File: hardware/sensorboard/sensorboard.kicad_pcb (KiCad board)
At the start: 2 copper layers, 48.9 x 19.3 mm, 23 parts, among them P1 PWR, P2 PROG, U1 ESP-07v2, U2 LMR16006Y, U3 BMP180_board, U4 DHT22

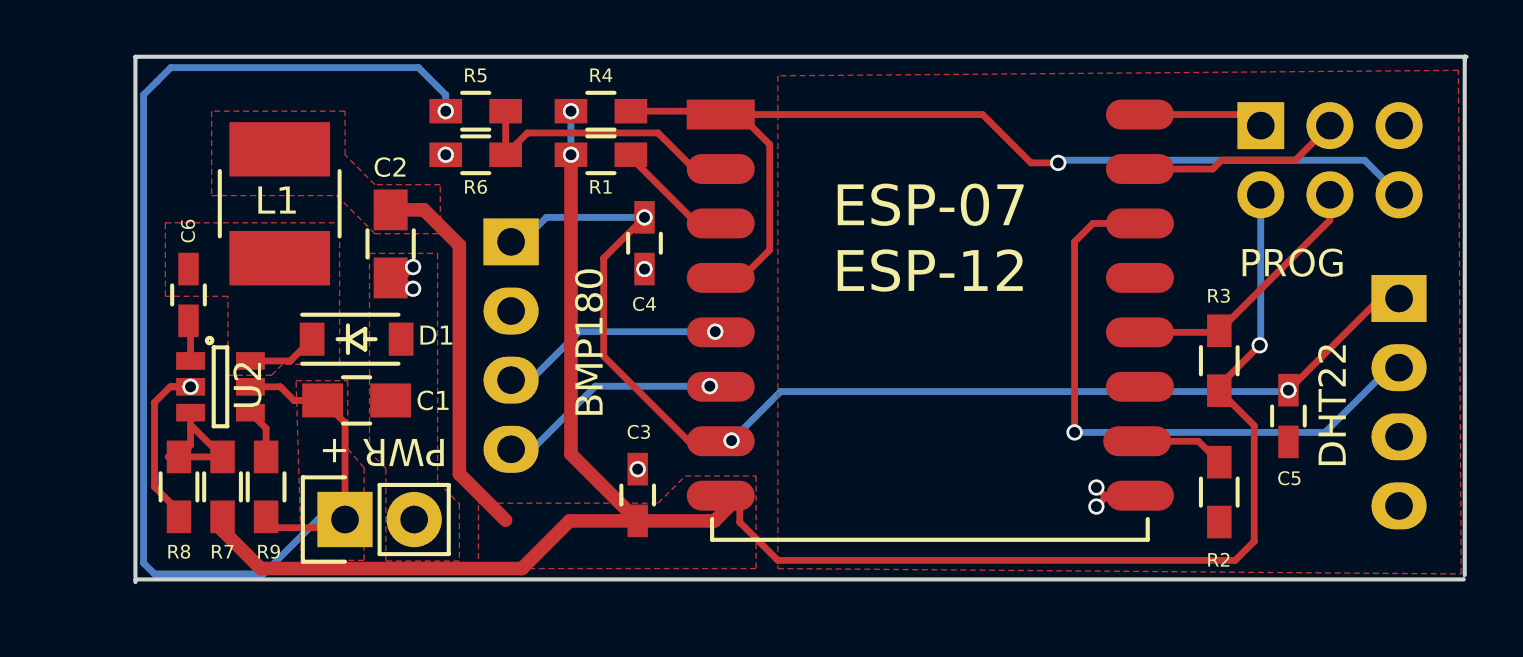
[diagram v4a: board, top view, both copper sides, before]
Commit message: Use bme280 for sensor - initial commit
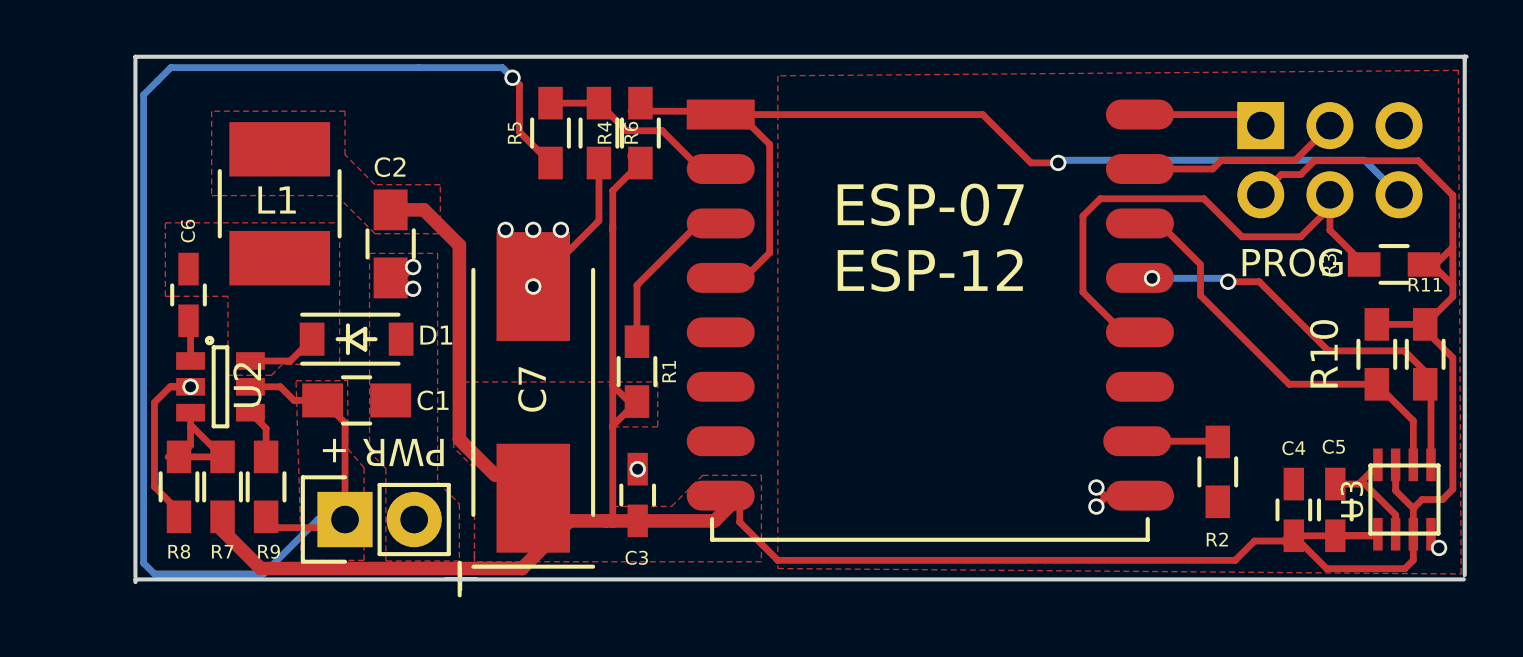
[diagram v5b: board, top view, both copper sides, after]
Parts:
- removed U4: DHT22, Pin_Headers:Pin_Header_Straight_1x04
- added C7: 100uf, Capacitors_Tantalum_SMD:TantalC_SizeD_EIA-7343_HandSoldering, F.Cu at (140.9, 84.7)
- added R10: 10k, Resistors_SMD:R_0603_HandSoldering, F.Cu at (171.9, 83.3)
- added R11: 10k, Resistors_SMD:R_0603_HandSoldering, F.Cu at (173.7, 83.3)
- U3: value BMP180_board -> BME280; footprint Pin_Headers:Pin_Header_Straight_1x04 -> TO_SOT_Packages_SMD:FGA8; moved to F.Cu
- moved U3 34.2 mm to (172.9, 88.7), turned to 0 degrees
- moved C4 25.8 mm to (168.9, 89.0), turned to 270 degrees
- moved R1 8.08 mm to (144.7, 84.0), turned to 90 degrees
- moved R3 7.33 mm to (172.5, 80.0), turned to 180 degrees
- moved R6 4.60 mm to (143.3, 75.2), turned to 270 degrees
- moved C5 3.85 mm to (170.4, 89.0), turned to 270 degrees
- moved R5 2.86 mm to (141.5, 75.2), turned to 90 degrees
- moved R4 1.66 mm to (144.9, 75.2), turned to 90 degrees
- moved R2 0.74 mm to (166.1, 87.6)
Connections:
- C4 pad 2: +3.3VP -> +3V3
- C5 pad 2: +3.3VP -> +3V3
- U1 pad 13: Net-(U1-Pad13) -> SDL
- U1 pad 14: GPIO4 -> SDA
- U1 pad 5: GPIO14 -> Net-(U1-Pad5)
- U1 pad 6: GPIO12 -> Net-(U1-Pad6)
- U1 pad 7: +3.3VP -> Net-(U1-Pad7)
- U3 pad 1: +3.3VP -> GND
- U3 pad 2: GND -> +3V3
- U3 pad 3: GPIO14 -> SDA
- U3 pad 4: GPIO12 -> SDL
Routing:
- net +3.3VP: track 44.3 -> 0.00 mm, vias 3 -> 0
- net +3V3: track 85.8 -> 111.5 mm, vias 3 -> 0
- net GPIO4: track 21.9 -> 0.00 mm, vias 1 -> 0
- net SDL: track 0.00 -> 16.5 mm, vias 0 -> 2
- net GND: track 11.4 -> 27.8 mm, vias 8 -> 11
- net SDA: track 0.00 -> 16.0 mm
- net GPIO12: track 9.36 -> 0.00 mm, vias 1 -> 0
- net GPIO14: track 9.14 -> 0.00 mm, vias 1 -> 0
- net GPIO0: track 10.3 -> 18.8 mm
- net +6V: track 48.8 -> 54.1 mm
- net CH_PD: track 5.10 -> 8.27 mm
- net ADC_IN: track 11.1 -> 9.63 mm
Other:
- board text removed: "BMP180"
- board text removed: "DATA"
- board text removed: "DHT22"
- board text removed: "SCL"
- board text removed: "SDA"
- board text removed: "VIN"

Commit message: Fix sensor placement and improve silkscreens
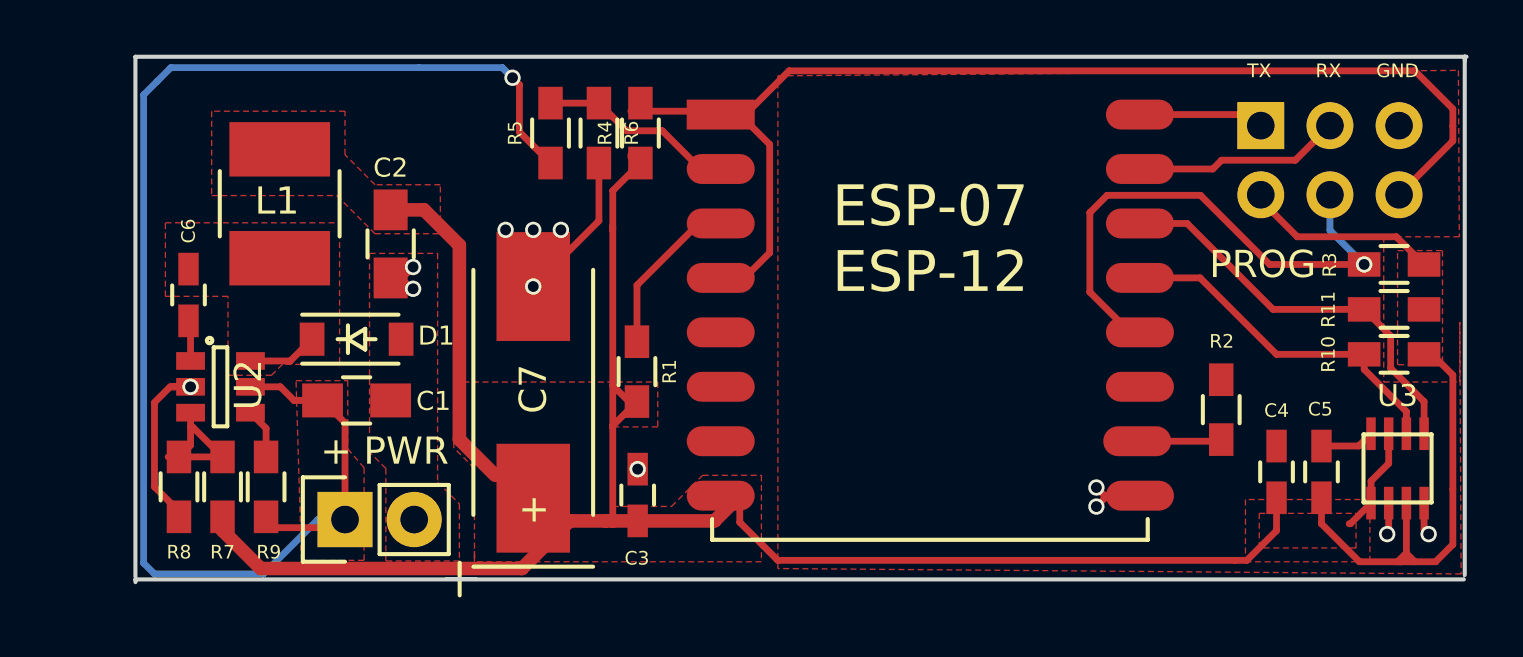
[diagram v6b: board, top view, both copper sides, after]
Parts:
- moved R2 2.29 mm to (166.2, 85.4), turned to 90 degrees
- moved R11 2.01 mm to (172.5, 81.7), turned to 0 degrees
- moved C4 1.53 mm to (168.2, 87.6)
- moved C5 1.49 mm to (169.9, 87.6)
- moved U3 1.17 mm to (172.7, 87.5)
- moved R10 0.64 mm to (172.5, 83.3), turned to 0 degrees
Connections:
- U1 pad 13: SDL -> SDA
- U1 pad 14: SDA -> SDL
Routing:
- net +3V3: track 111.5 -> 100.7 mm
- net GPIO16: track 36.6 -> 42.5 mm, vias 1 -> 0
- net SDA: track 16.0 -> 14.8 mm
- net GPIO0: track 18.8 -> 19.9 mm, vias 0 -> 1
- net SDL: track 16.5 -> 17.1 mm, vias 2 -> 0
- net GND: track 27.8 -> 27.4 mm, vias 11 -> 12
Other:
- board text added: "+ PWR"
- board text added: "ESP sensorboard v4.0"
- board text added: "RX"
- board text added: "TX"
- board text removed: "ESP sensorboard v3.1"
- board text removed: "PWR +"

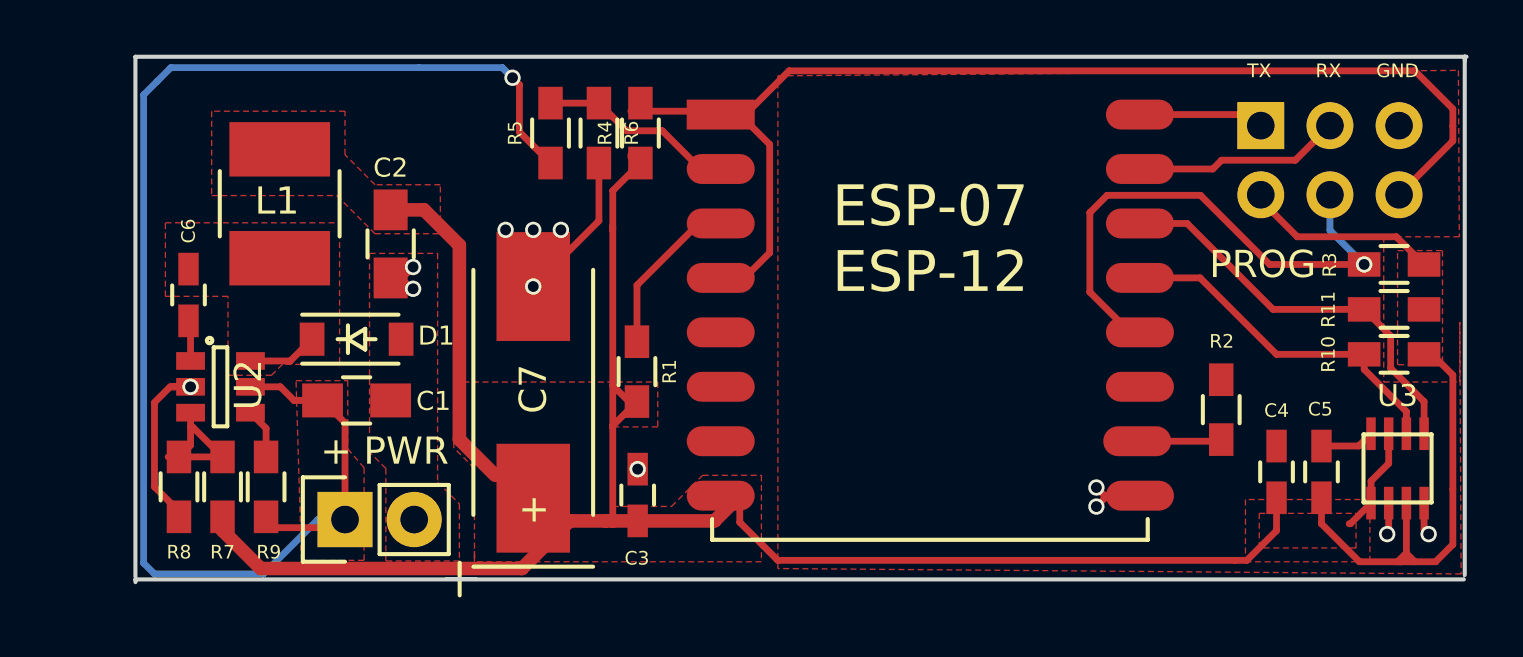
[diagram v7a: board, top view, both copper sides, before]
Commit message: Fixed some silkscreens, added BOM.
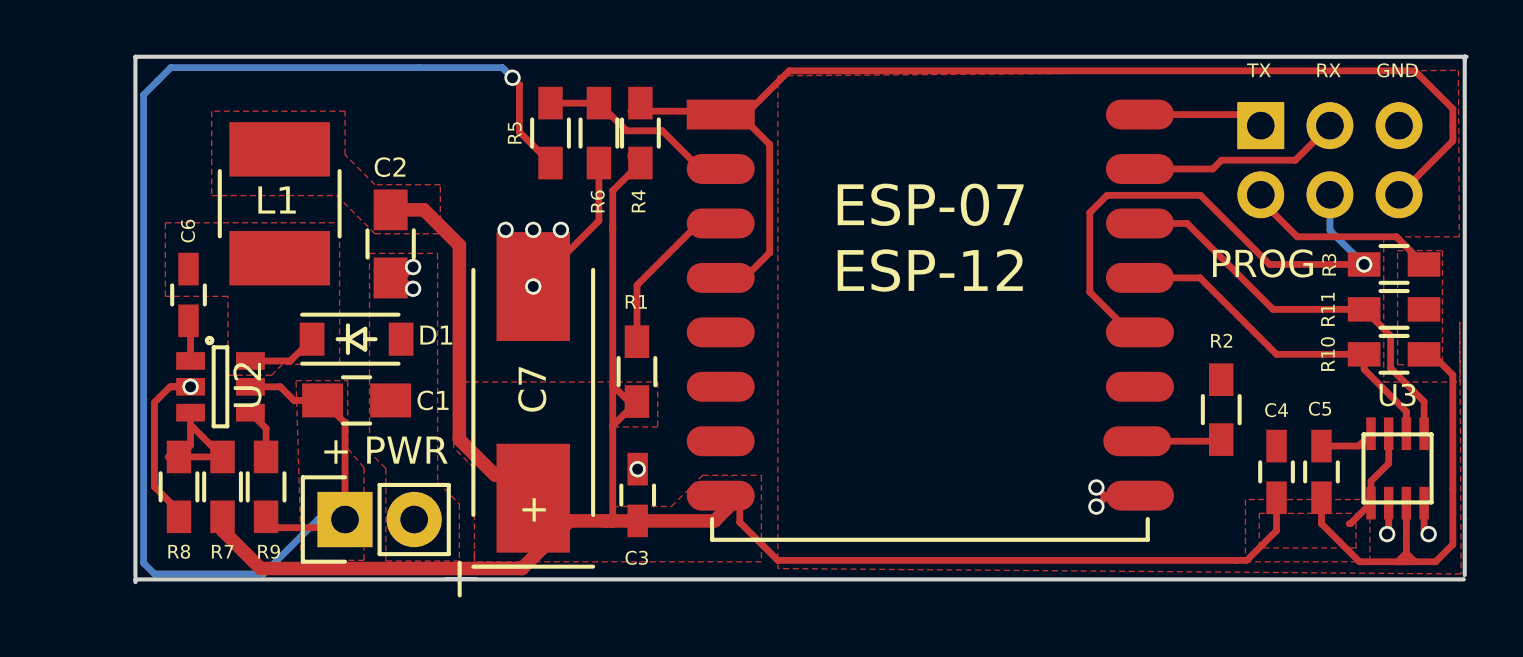
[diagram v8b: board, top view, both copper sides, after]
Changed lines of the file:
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@@
     (links 58)
     (no_connects 0)
-    (area 126.224999 72.314999 175.275001 91.775001)
+    (area 124.864286 65.548599 175.300906 92.461041)
     (thickness 1.6)
     (drawings 14)
@@
     (tags "resistor 0603")
     (attr smd)
-    (fp_text reference R4 (at 0 -1.3 90) (layer F.SilkS)
+    (fp_text reference R4 (at -2.52 -0.051 90) (layer F.SilkS)
       (effects (font (size 0.5 0.5) (thickness 0.1)))
     )
@@
     (tags "resistor 0603")
     (attr smd)
-    (fp_text reference R1 (at 0 1.2 90) (layer F.SilkS)
+    (fp_text reference R1 (at 2.543 -0.024 180) (layer F.SilkS)
       (effects (font (size 0.5 0.5) (thickness 0.1)))
     )
@@
     (tags "resistor 0603")
     (attr smd)
-    (fp_text reference R6 (at 0 -1.2 270) (layer F.SilkS)
-      (effects (font (size 0.5 0.5) (thickness 0.1)))
-    )
+    (fp_text reference R6 (at 2.52 0.027 270) (layer F.SilkS)
+      (effects (font (size 0.5 0.5) (thickness 0.1)))
+    )
